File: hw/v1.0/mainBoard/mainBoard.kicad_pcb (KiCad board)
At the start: 2 copper layers, 50 x 100 mm, 121 parts, among them J10 BAT+, J15 U.FL, J4 PROGRAMMER, J6 EN_3V3_PROGRAMMER, J8 PMS5003, J9 BAT-, Q1 MMBT3904, Q10 AO3401A, Q11 2N7002, Q12 AO3401A, Q13 2N7002, Q14 AO3401A, Q15 2N7002, Q16 2N7002, Q17 2N7002, Q2 MMBT3904, Q3 AO3401A, Q4 2N7002, Q5 AO3401A, Q6 2N7002, Q9 AO3401A, SW1 PWR_ON, SW2 PWR_OFF, SW3 RESET, SW4 SW_Push, U1 ESP32-WROOM-32, U10 AP1603, U2 MCP3202-BI/SN, U3 AMS1117-3.3, U4 VEML7700, U5 RFM95W-868S2, U6 ML8511, U7 BMP388, U8 SGP30, U9 SHT40

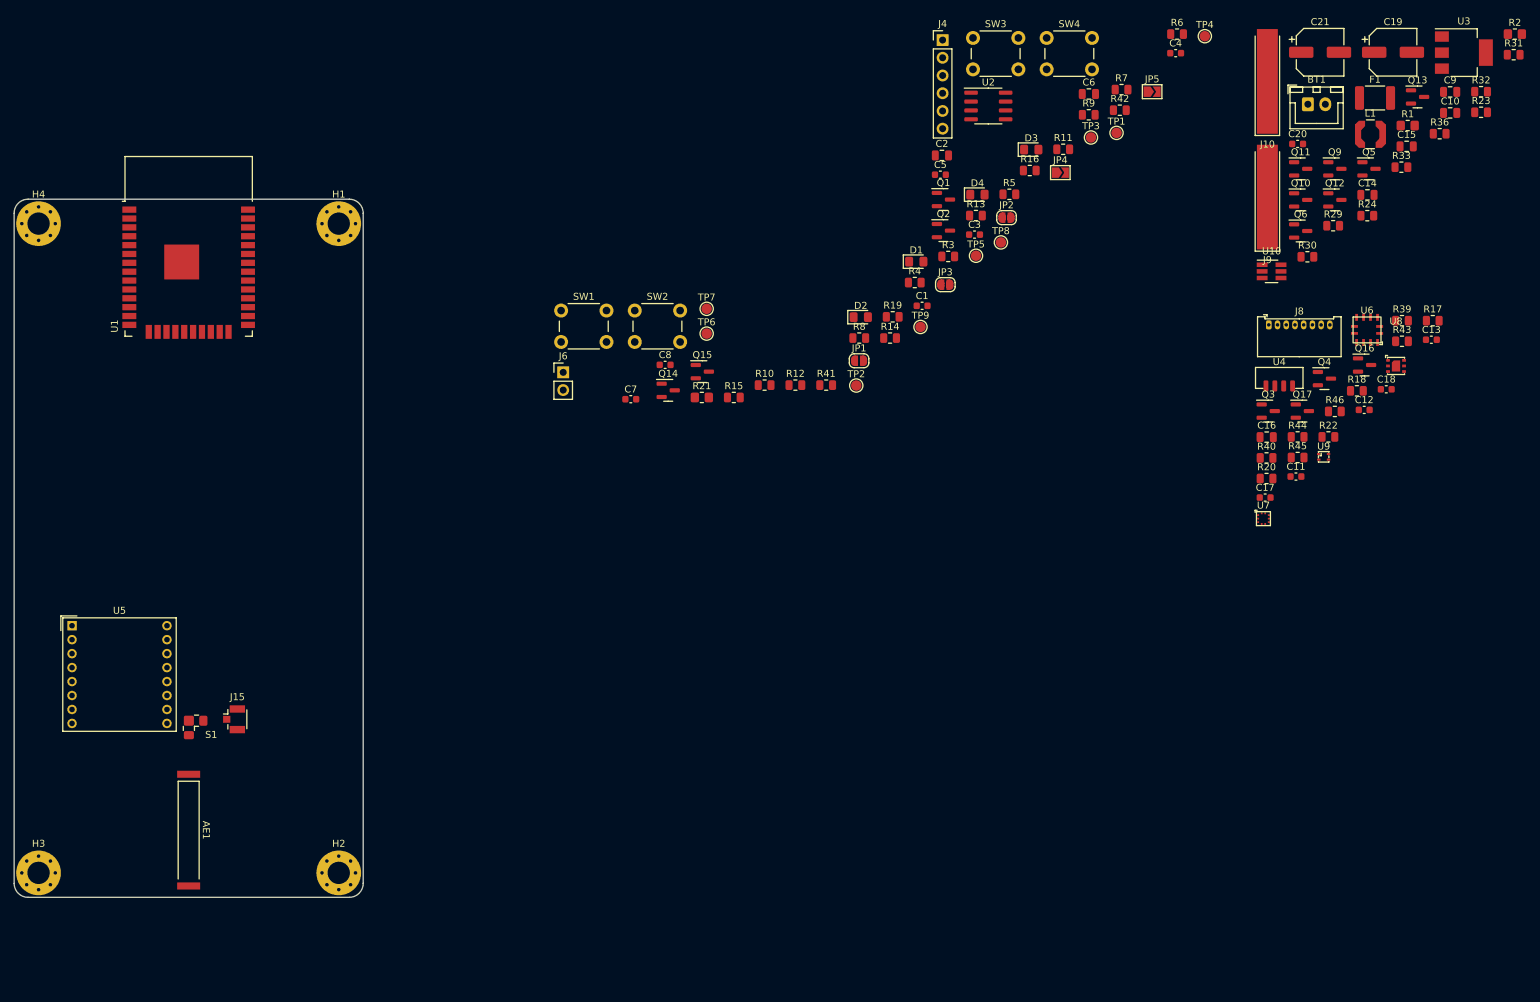
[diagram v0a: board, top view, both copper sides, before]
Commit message: More component placement in mainboard
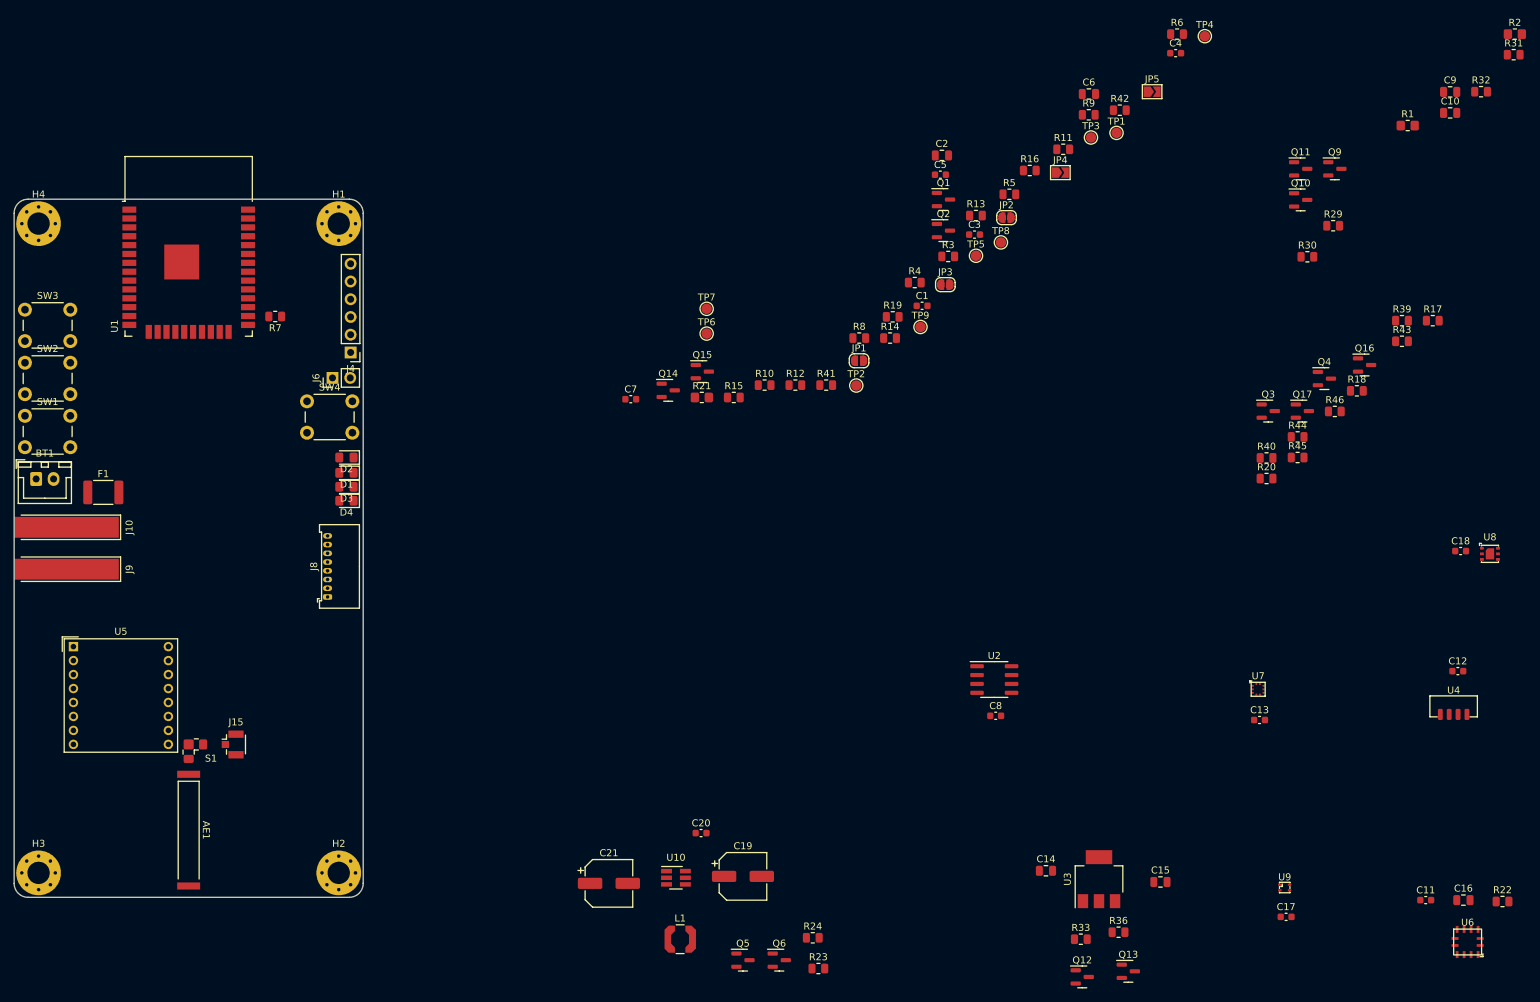
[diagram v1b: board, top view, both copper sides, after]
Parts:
- moved J10 193.2 mm to (65.0, 89.0), turned to 90 degrees
- moved F1 190.7 mm to (77.8, 84.0)
- moved BT1 189.9 mm to (68.2, 82.1)
- moved J9 189.5 mm to (65.0, 95.0), turned to 90 degrees
- moved C21 156.7 mm to (150.2, 140.0)
- moved R23 155.1 mm to (180.2, 152.2)
- moved L1 151.9 mm to (160.4, 148.0)
- moved C19 150.4 mm to (169.4, 139.0)
- moved Q5 144.5 mm to (169.4, 151.0)
- moved SW3 141.3 mm to (66.5, 57.8)
- moved J8 140.3 mm to (109.9, 99.0), turned to 90 degrees
- moved Q13 131.9 mm to (224.6, 152.6)
- moved C20 130.6 mm to (163.4, 132.8)
- moved R24 130.4 mm to (179.4, 147.8)
- moved U3 129.4 mm to (220.4, 139.4), turned to 90 degrees
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
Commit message: More component placement in mainboard
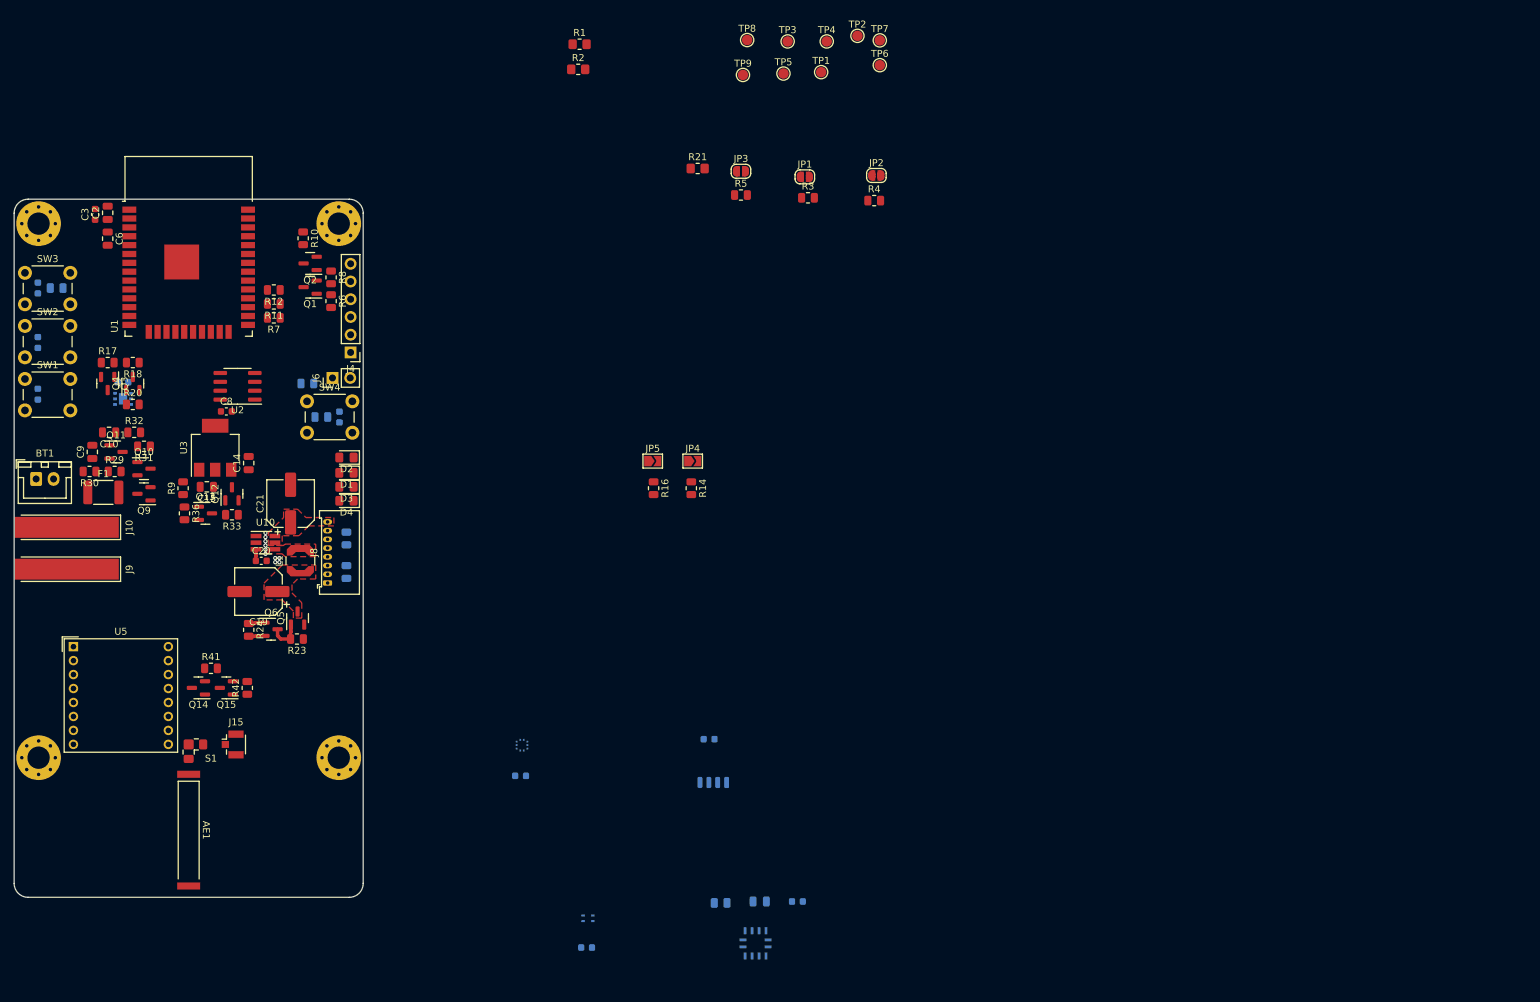
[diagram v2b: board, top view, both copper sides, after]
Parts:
- removed Q16, Q17: 2N7002, Package_TO_SOT_SMD:SOT-23
- removed R43, R44, R45, R46: 100k, Resistor_SMD:R_0805_2012Metric
- C1, C11, C12, C13, C16, C17, C18, C4, C5, C7, R13, R15, R19, R22, R39, R40, U4, U6, U7, U8, U9: moved to B.Cu
- moved R31 204.1 mm to (83.6, 77.4), turned to 180 degrees
- moved C9 201.2 mm to (76.2, 78.2), turned to 90 degrees
- moved R32 199.0 mm to (82.2, 75.4)
- moved C10 197.5 mm to (78.6, 75.4), turned to 180 degrees
- moved U8 197.1 mm to (80.6, 70.6), turned to 180 degrees
- moved C18 193.1 mm to (80.6, 68.2), turned to 180 degrees
- moved R17 189.9 mm to (78.4, 65.4)
- moved R29 178.1 mm to (79.4, 81.0)
- moved R30 177.1 mm to (75.8, 81.0), turned to 180 degrees
- moved Q9 176.8 mm to (83.6, 84.2), turned to 180 degrees
- moved R18 175.4 mm to (82.0, 65.4), turned to 180 degrees
- moved Q11 174.5 mm to (79.6, 78.2)
- moved Q4 170.7 mm to (82.0, 68.4), turned to 90 degrees
- moved Q10 170.1 mm to (83.6, 80.6)
- moved C4 168.2 mm to (68.4, 62.5), turned to -90 degrees
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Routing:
- net Net-(Q5-Pad1): track 0.00 -> 5.07 mm
- net +5V_EN: track 0.00 -> 2.31 mm
- net GND: track 0.00 -> 2.28 mm, vias 0 -> 10
- net Net-(C20-Pad1): track 0.00 -> 1.66 mm
- added copper zone on F.Cu, net +5V
- added copper zone on F.Cu, net Net-(C19-Pad1)
- added copper zone on F.Cu, net Net-(L1-Pad2)

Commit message: Maybe final component placement
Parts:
- added C22: 1u, Capacitor_SMD:C_0805_2012Metric, F.Cu at (86.2, 66.4)
- added C23: 1u, Capacitor_SMD:C_0805_2012Metric, F.Cu at (85.2, 72.8)
- added Q7: 2N7002, Package_TO_SOT_SMD:SOT-23, B.Cu at (85.8, 62.6)
- added Q8: 2N7002, Package_TO_SOT_SMD:SOT-23, B.Cu at (82.0, 75.0)
- added R25: 100k, Resistor_SMD:R_0805_2012Metric, B.Cu at (85.8, 65.6)
- added R26: 100k, Resistor_SMD:R_0805_2012Metric, B.Cu at (82.0, 72.0)
- added R27: 100k, Resistor_SMD:R_0805_2012Metric, B.Cu at (83.0, 62.6)
- added R28: 100k, Resistor_SMD:R_0805_2012Metric, B.Cu at (79.2, 75.0)
- added U11: NCP115ASN180T2G, Package_SO:TSOP-5_1.65x3.05mm_P0.95mm, F.Cu at (85.2, 70.0)
- JP1, JP2, JP3, R21, R3, R4, R5: moved to B.Cu
- moved C11 109.6 mm to (100.4, 64.4)
- moved U6 107.1 mm to (100.0, 68.6)
- moved R22 104.6 mm to (97.8, 63.6), turned to -90 degrees
- moved C16 99.6 mm to (100.6, 73.0)
- moved C17 99.0 mm to (88.6, 69.2), turned to 90 degrees
- moved R1 94.3 mm to (86.0, 92.5), turned to -90 degrees
- moved U9 94.2 mm to (91.2, 69.2)
- moved JP2 92.2 mm to (105.6, 79.0)
- moved R2 89.8 mm to (88.5, 92.5), turned to 90 degrees
- moved R4 87.3 mm to (109.0, 79.0)
- moved JP1 84.3 mm to (105.6, 81.6)
- moved R3 80.1 mm to (109.0, 81.2)
- moved JP3 78.5 mm to (105.6, 84.2)
- moved U4 77.7 mm to (100.0, 81.6)
- moved R5 73.2 mm to (109.0, 83.2)
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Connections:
- Q3 pad 3: SGP_VDD -> Net-(C23-Pad1)
- R1 pad 1: VDD_IN -> 3V3
- U8 pad 3: SDA -> SDA_1V8
- U8 pad 6: SCL -> SCL_1V8
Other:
- board text added: "I2C PullUp"

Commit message: Start routing mainBoard
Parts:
- R21: footprint Resistor_SMD:R_0805_2012Metric_Pad1.20x1.40mm_HandSolder -> Resistor_SMD:R_0805_2012Metric
- moved R11 1.17 mm to (102.8, 58.0)
- moved R12 1.17 mm to (102.8, 56.0)
- moved R7 1.17 mm to (102.8, 60.0)
- moved R21 0.20 mm to (109.0, 85.2)
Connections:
- JP4 pad 1: SDA -> Net-(JP4-Pad1)
- JP4 pad 2: Net-(JP4-Pad2) -> SDA
- R14 pad 2: Net-(JP4-Pad2) -> Net-(JP4-Pad1)
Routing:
- net GND: track 2.28 -> 28.2 mm
- net SGP_VDD: track 0.00 -> 22.3 mm, vias 0 -> 2
- net RX: track 0.00 -> 19.0 mm, vias 0 -> 1
- net TX: track 0.00 -> 18.4 mm, vias 0 -> 1
- net PWR_OFF: track 0.00 -> 17.9 mm
- net RTS: track 0.00 -> 15.4 mm
- net SEN_VDD: track 0.00 -> 13.6 mm
- net SWITCH: track 0.00 -> 10.5 mm
- net IO0: track 0.00 -> 10.2 mm, vias 0 -> 2
- net Net-(C5-Pad1): track 0.00 -> 10.1 mm
- net PWR_ON: track 0.00 -> 8.17 mm
- net SDA: track 0.00 -> 6.79 mm
- net EN: track 0.00 -> 6.36 mm
- net SCL: track 0.00 -> 6.00 mm
- net SCL_1V8: track 0.00 -> 5.29 mm, vias 0 -> 2
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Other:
- board text added: "I2C Pull-Up Enable"
- board text removed: "I2C PullUp"

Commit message: More routing at mainBoard
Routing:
- net GND: track 28.2 -> 44.1 mm
- net +5V: track 0.00 -> 9.46 mm
- net Net-(C23-Pad1): track 0.00 -> 8.40 mm
- net Net-(Q3-Pad1): track 0.00 -> 6.23 mm, vias 0 -> 2
- net Net-(Q4-Pad1): track 0.00 -> 6.03 mm
- net Net-(C14-Pad1): track 0.00 -> 5.05 mm
- net Net-(Q12-Pad1): track 0.00 -> 4.12 mm
- net 3V3: track 4.98 -> 7.05 mm
- net ADC_1: track 0.00 -> 2.05 mm, vias 0 -> 1
- net SGP_VDD: track 22.3 -> 24.1 mm
- added copper zone on F.Cu, net 3V3_L
- added copper zone on F.Cu, net Net-(BT1-Pad1)
- added copper zone on F.Cu, net VDD_IN

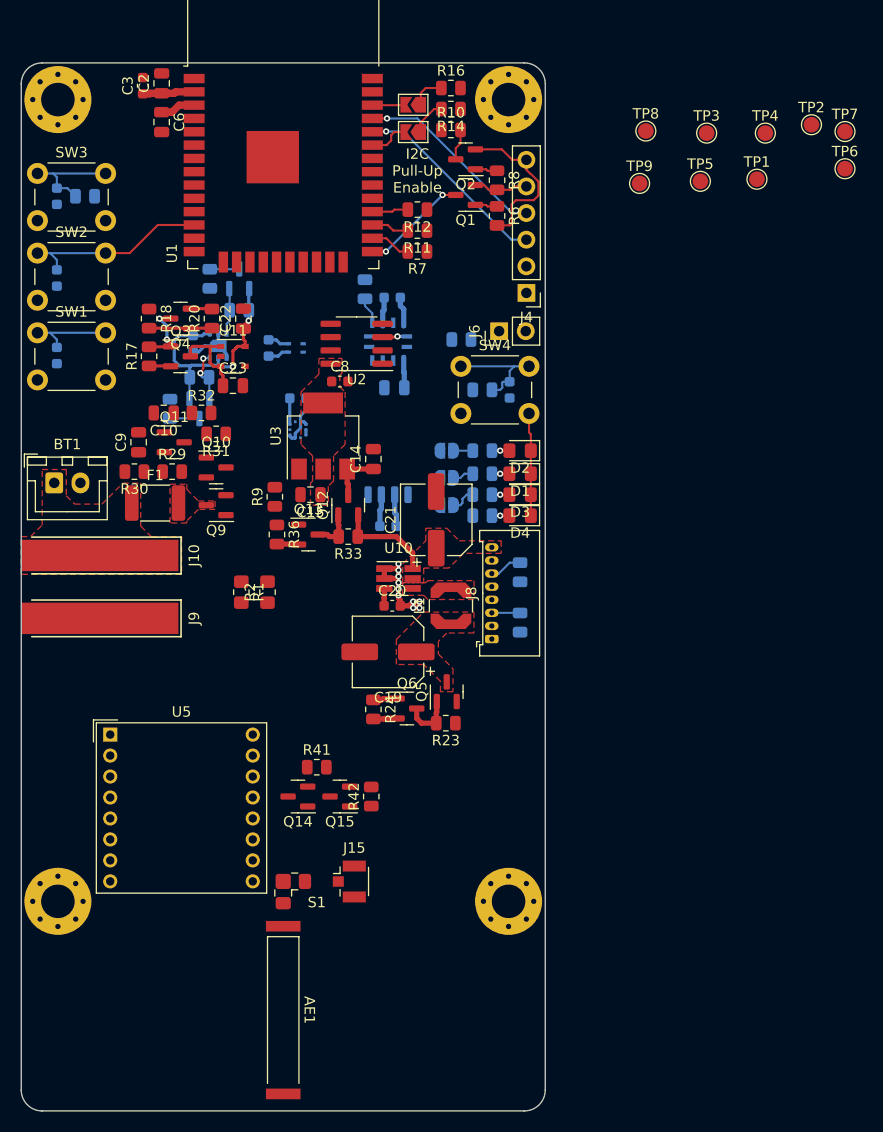
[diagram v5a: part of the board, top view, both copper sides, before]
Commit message: Maybe finished first component placement and routing mainBoard
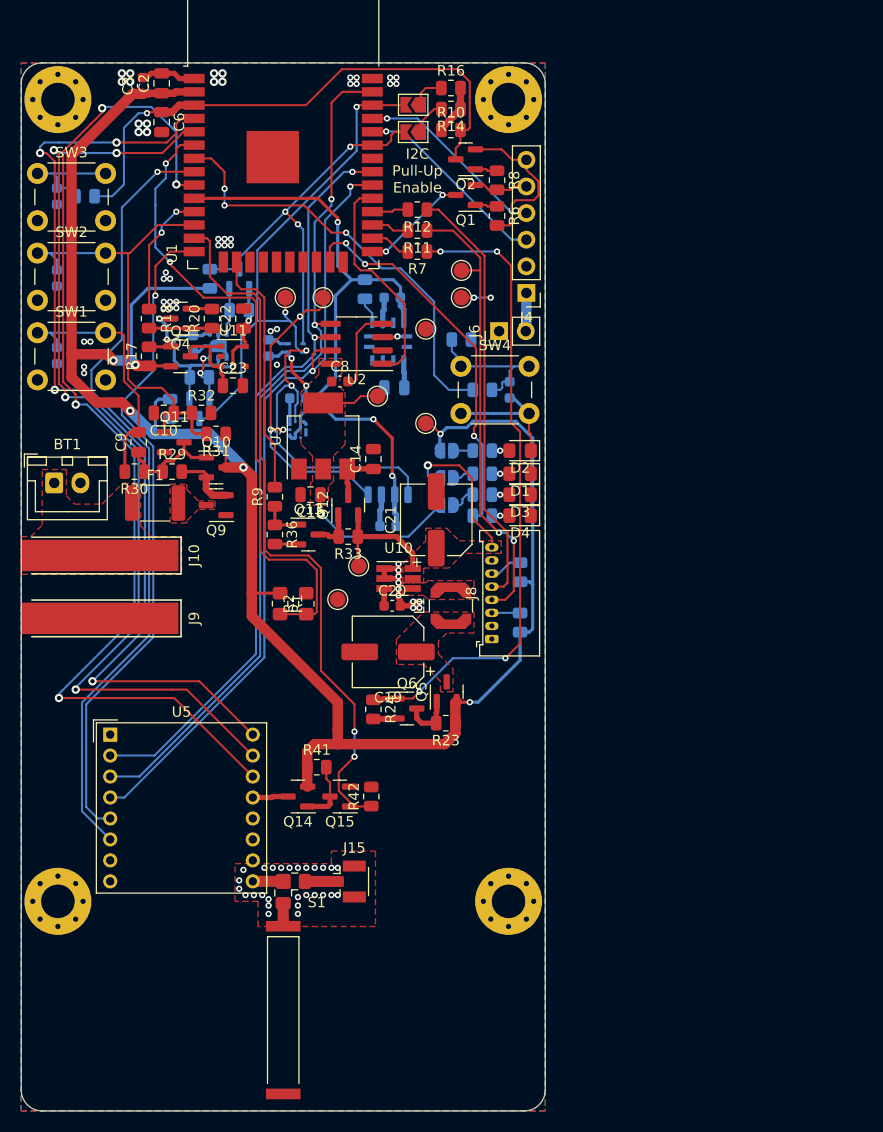
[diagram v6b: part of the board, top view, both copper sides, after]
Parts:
- moved TP8 53.5 mm to (95.2, 93.2)
- moved TP2 52.8 mm to (90.2, 64.4)
- moved TP7 51.3 mm to (99.0, 73.8)
- moved TP5 49.1 mm to (97.2, 90.0)
- moved TP6 46.8 mm to (103.6, 76.4)
- moved TP1 42.9 mm to (93.8, 64.4)
- moved TP4 33.0 mm to (107.0, 64.4)
- moved TP3 26.8 mm to (107.0, 61.8)
- moved TP9 24.7 mm to (103.6, 67.4)
- moved R1 3.86 mm to (89.7, 93.6)
- moved R2 3.86 mm to (92.2, 93.6)
- moved R36 0.20 mm to (89.2, 87.0)
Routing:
- net 3V3: track 7.05 -> 192.0 mm, vias 0 -> 6
- net DIO0: track 0.00 -> 100.8 mm, vias 0 -> 4
- net DIO2: track 0.00 -> 93.0 mm, vias 0 -> 4
- net DIO1: track 0.00 -> 92.9 mm, vias 0 -> 4
- net MOSI: track 0.00 -> 82.0 mm, vias 0 -> 2
- net SCL: track 6.00 -> 84.5 mm, vias 0 -> 4
- net LORA_RST: track 0.00 -> 75.9 mm, vias 0 -> 1
- net SCLK: track 0.00 -> 75.3 mm, vias 0 -> 2
- net MISO: track 0.00 -> 73.1 mm, vias 0 -> 2
- net LORA_EN: track 0.00 -> 68.0 mm, vias 0 -> 2
- net CS_LORA: track 0.00 -> 63.8 mm, vias 0 -> 1
- net SDA: track 6.79 -> 68.7 mm, vias 0 -> 6
- net ADC_VIN: track 0.00 -> 61.6 mm, vias 0 -> 2
- net SEN_VDD: track 13.6 -> 73.6 mm, vias 0 -> 5
- net +5V_EN: track 2.31 -> 61.2 mm, vias 0 -> 4
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- added copper zone on B.Cu, net GND
- added copper zone on F.Cu, net GND
